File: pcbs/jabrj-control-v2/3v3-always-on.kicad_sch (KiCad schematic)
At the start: 7 parts, among them U501 TPS7B8133QDRVRQ1, U502 TPS2116DRL

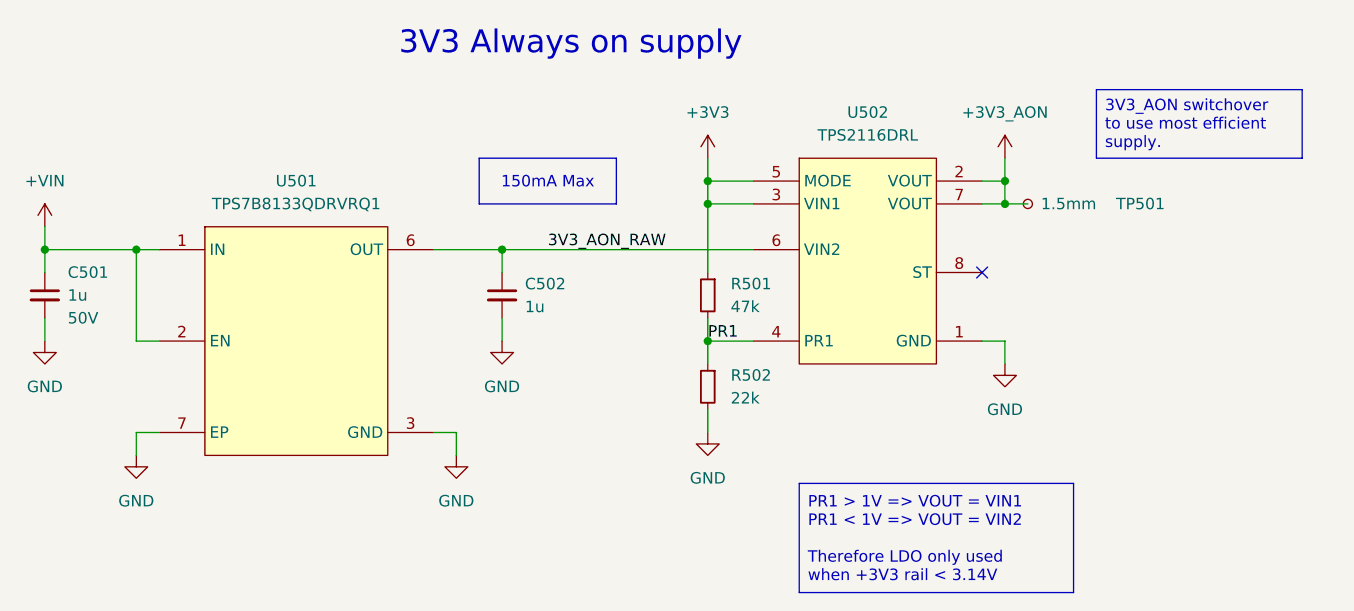
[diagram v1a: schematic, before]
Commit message: Minor schematic fixes
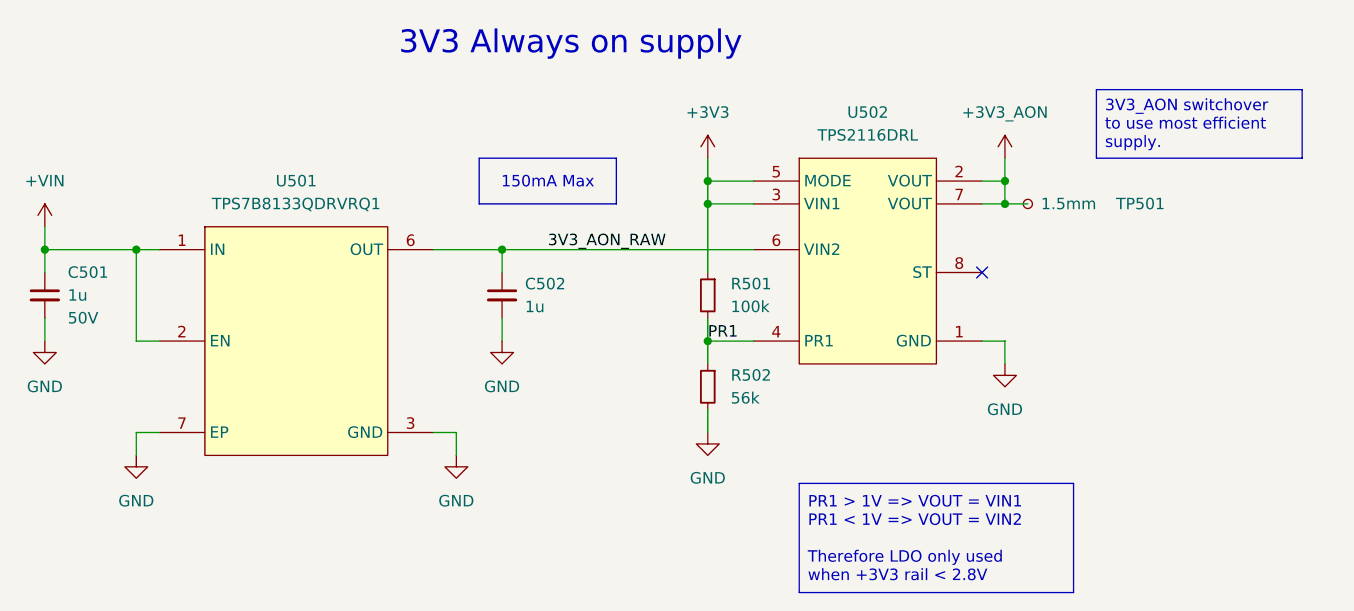
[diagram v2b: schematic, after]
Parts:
- R501: value 47k -> 100k
- R502: value 22k -> 56k
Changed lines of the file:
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@@
 		)
 	)
-	(text_box "PR1 > 1V => VOUT = VIN1\nPR1 < 1V => VOUT = VIN2\n\nTherefore LDO only used when +3V3 rail < 3.14V"
+	(text_box "PR1 > 1V => VOUT = VIN1\nPR1 < 1V => VOUT = VIN2\n\nTherefore LDO only used when +3V3 rail < 2.8V"
 		(exclude_from_sim no)
 		(at 167.64 122.4932 0)
@@
 			)
 		)
-		(property "Value" "47k"
+		(property "Value" "100k"
 			(at 160.02 102.8699 0)
 			(show_name no)
@@
 			)
 		)
-		(property "Value" "22k"
+		(property "Value" "56k"
 			(at 160.02 113.0299 0)
 			(show_name no)
